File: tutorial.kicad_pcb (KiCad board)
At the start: 2 copper layers, 178.2 x 165.7 mm, 73 parts

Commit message: routing done!
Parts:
- moved _5 28.1 mm to (118.9, 99.1), turned to 0 degrees
- moved ROT1 27.8 mm to (108.9, 109.7), turned to 0 degrees
- moved S4 24.9 mm to (108.9, 127.1), turned to 0 degrees
- moved _4 24.2 mm to (173.1, 91.5), turned to -0.5 degrees
- moved D4 24.1 mm to (108.9, 132.1), turned to 180 degrees
- moved S9 24.0 mm to (133.7, 107.8), turned to 0 degrees
- moved D9 22.9 mm to (133.7, 112.8), turned to 180 degrees
- moved S3 22.3 mm to (108.9, 146.4), turned to 0 degrees
- moved D3 21.8 mm to (108.9, 151.4), turned to 180 degrees
- moved S14 21.4 mm to (153.6, 107.8), turned to -0.5 degrees
- moved S19 20.6 mm to (173.0, 105.5), turned to -0.5 degrees
- moved S2 20.6 mm to (108.9, 165.7), turned to 0 degrees
- moved D2 20.4 mm to (108.9, 170.7), turned to 180 degrees
- moved D14 20.3 mm to (153.6, 112.8), turned to 179.5 degrees
- moved D1 20.2 mm to (108.9, 190.0), turned to 180 degrees
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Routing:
- net GND: track 0.00 -> 451.7 mm, vias 0 -> 7
- net GP4: track 0.00 -> 328.0 mm, vias 0 -> 6
- net GP1: track 0.00 -> 323.7 mm, vias 0 -> 5
- net GP16: track 0.00 -> 321.9 mm, vias 0 -> 3
- net GP17: track 0.00 -> 313.2 mm, vias 0 -> 1
- net GP5: track 0.00 -> 308.7 mm, vias 0 -> 6
- net GP8: track 0.00 -> 300.1 mm, vias 0 -> 8
- net GP6: track 0.00 -> 293.1 mm, vias 0 -> 6
- net GP7: track 0.00 -> 287.0 mm, vias 0 -> 7
- net GP13: track 0.00 -> 201.4 mm, vias 0 -> 1
- net GP12: track 0.00 -> 169.8 mm, vias 0 -> 1
- net GP9: track 0.00 -> 169.2 mm, vias 0 -> 1
- net GP10: track 0.00 -> 161.6 mm, vias 0 -> 1
- net GP11: track 0.00 -> 156.0 mm, vias 0 -> 1
- net GP14: track 0.00 -> 116.7 mm, vias 0 -> 1
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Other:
- board size 178.2 x 165.7 mm -> 162.7 x 143.3 mm

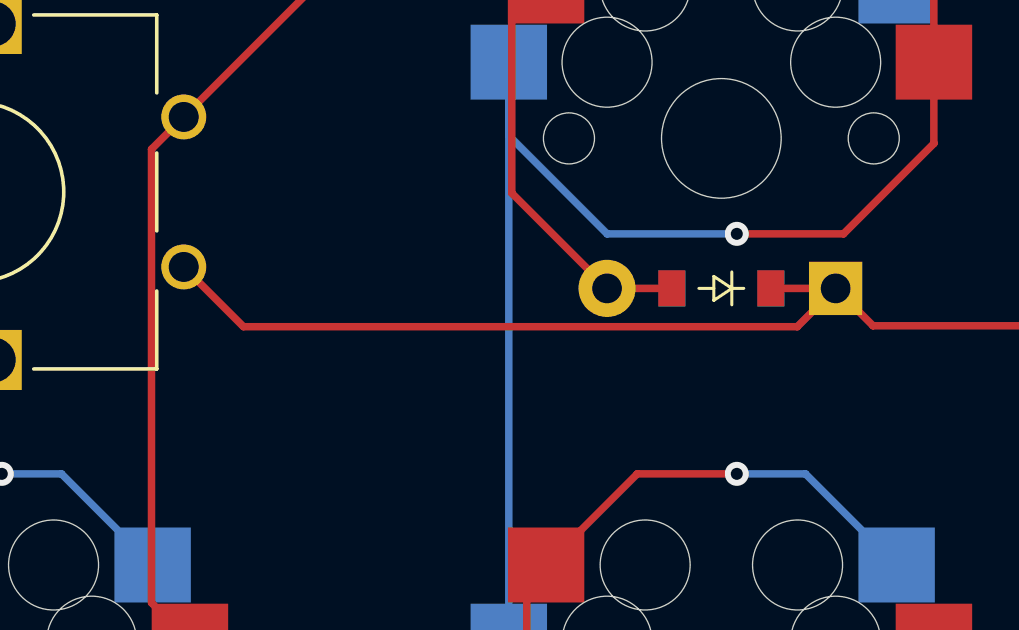
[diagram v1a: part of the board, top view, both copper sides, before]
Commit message: added an diode for the encoder
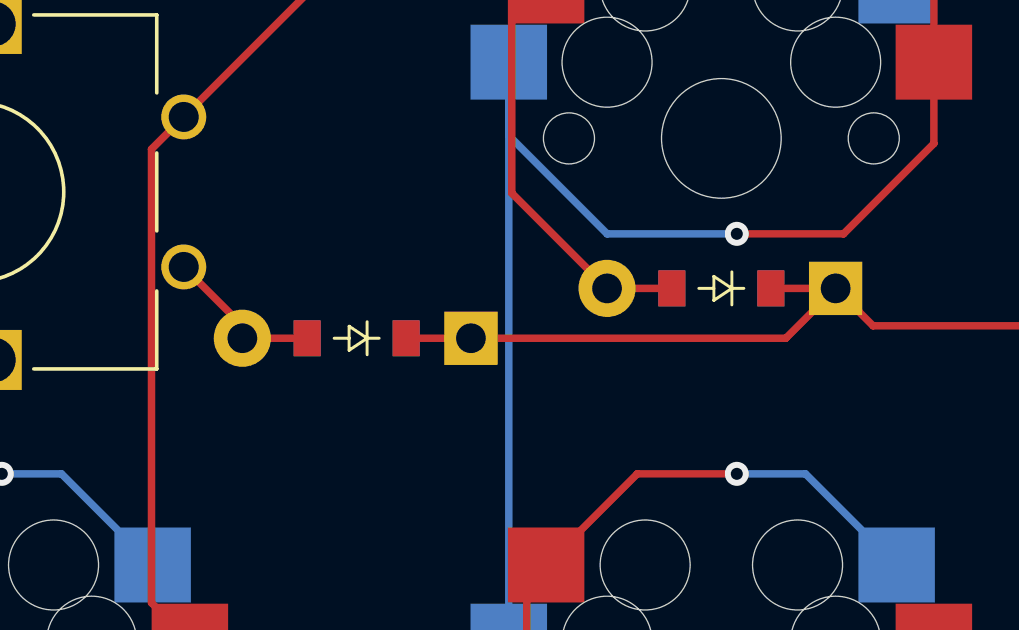
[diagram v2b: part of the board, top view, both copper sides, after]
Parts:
- added D4: , ComboDiode, F.Cu at (121.5, 114.5)
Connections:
- ROT1 pad 2: GP9 -> enc
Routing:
- net GP9: track 169.2 -> 161.1 mm
- net enc: track 0.00 -> 5.35 mm
